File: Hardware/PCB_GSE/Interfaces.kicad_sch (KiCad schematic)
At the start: 32 parts, among them J21 BM03B-GHS-TBT, J3 Screw_Terminal_01x04, J4 GT17HN-4DP-2H(D)(56), J5 Conn_02x07_Odd_Even, J6 Conn_01x02, U5 SI5442DU-T1-GE3, U6 SI5442DU-T1-GE3, U7 SI5442DU-T1-GE3, U8 ISOW1044

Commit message: fix : done silkscreen and finition
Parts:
- renumbered C52 to C1, C50 to C10, C51 to C11, C48 to C12, C53 to C2, C47 to C23, C45 to C25, C55 to C3, C54 to C4, C56 to C5, C46 to C8, C49 to C9, D3 to D1, D1 to D2, FB4 to FB1, J6 to J1, J21 to J2, J4 to J3, J3 to J5, R42 to R1, R40 to R11, R41 to R12, R36 to R14, R38 to R15, R43 to R2, R6 to R3, R7 to R5, U8 to U2, U6 to U3, U7 to U6, U5 to U7, J5 to X1
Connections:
- net GND: no longer J3.5 (Shell)
- no-connect marks 3 -> 4

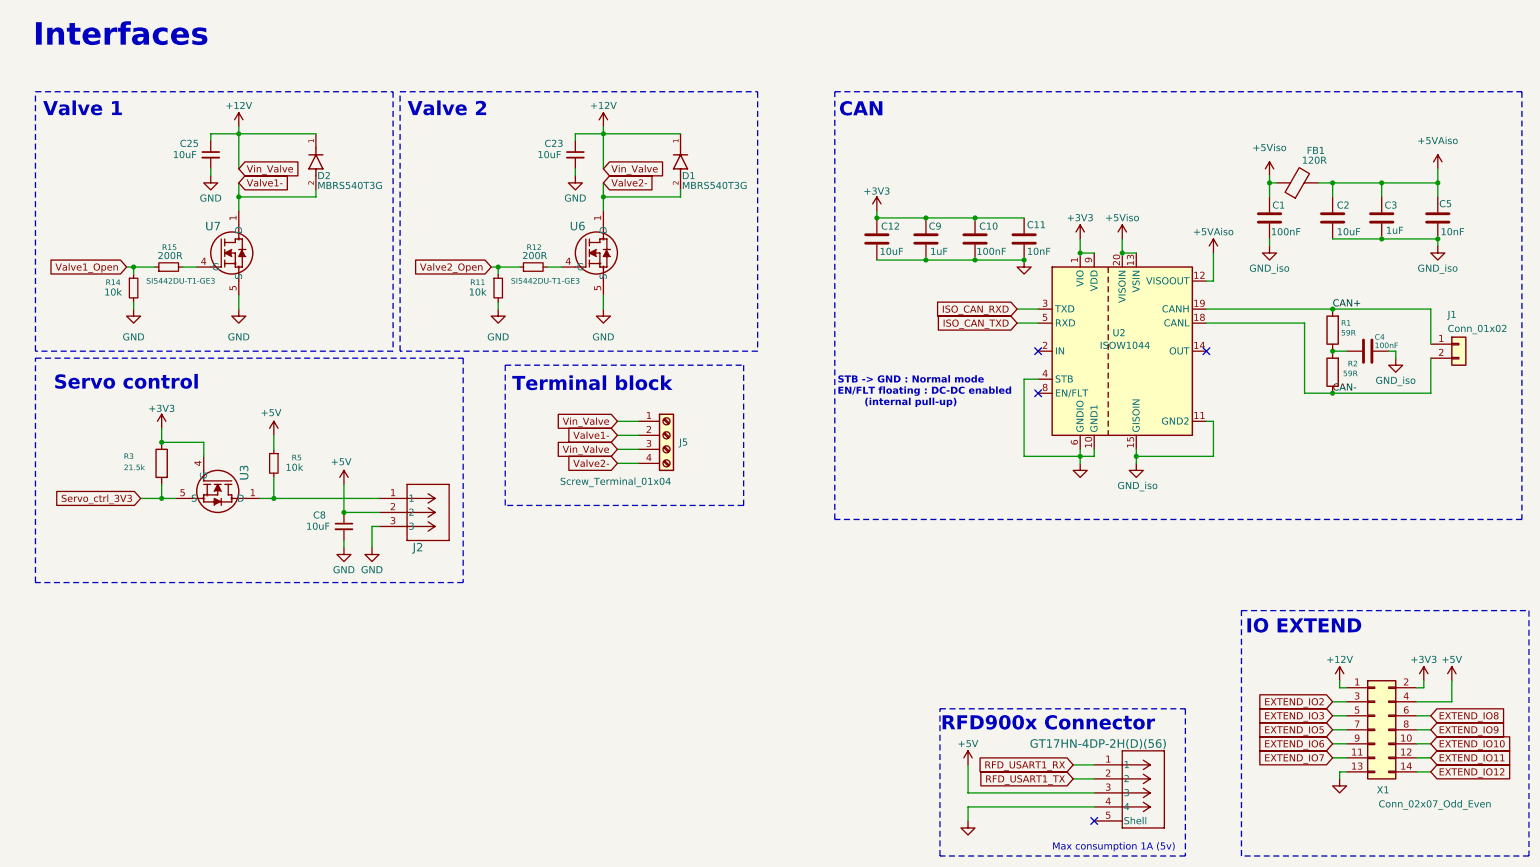
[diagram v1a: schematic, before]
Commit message: fix(gse): Vin servo
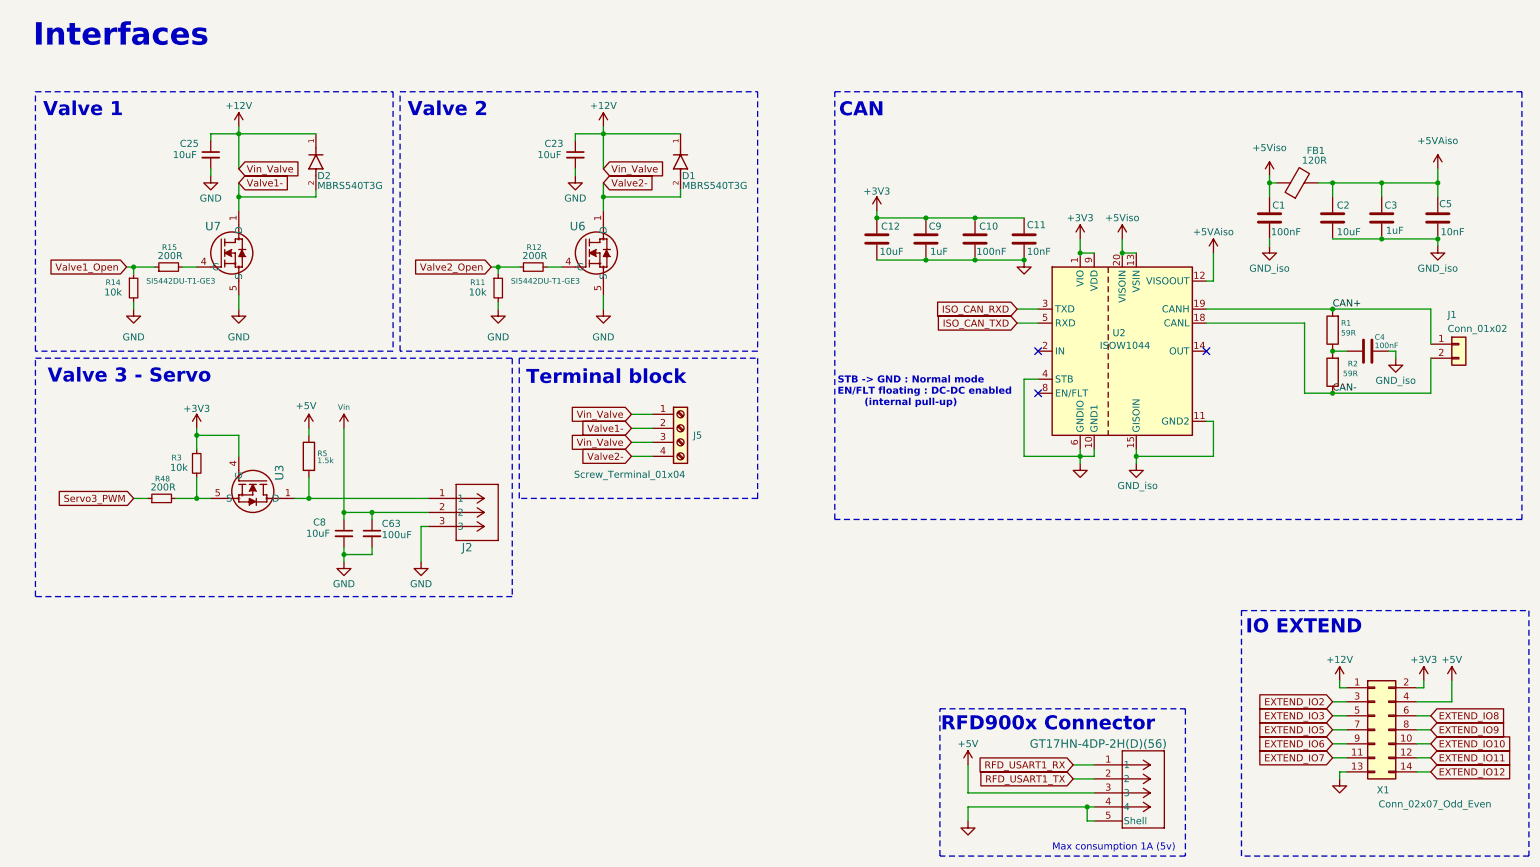
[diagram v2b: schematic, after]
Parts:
- removed R3: 21.5k, Resistor_SMD:R_0805_2012Metric, symbol Device:R
- removed R5: 10k, Resistor_SMD:R_0805_2012Metric, symbol Device:R_Small
- added C63: 100uF, Capacitor_SMD:C_0805_2012Metric, symbol Device:C_Small
- added R3: 10k, Resistor_SMD:R_0805_2012Metric, symbol Device:R_Small
- added R48: 200R, Resistor_SMD:R_0805_2012Metric, symbol Device:R_Small
- added R5: 1.5k, Resistor_SMD:R_0805_2012Metric, symbol Device:R
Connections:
- net +3V3: now also R3.1
- net +5V: now also R5.1; no longer C8.1, J2.2
- net GND: now also J3.5 (Shell), C63.2
- net at J2.1, U3.1 (D), U3.2 (D)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: now also R5.2
- net Servo_ctrl_3V3: no longer names the net of U3.5 (S), U3.9 (S)
- net Servo_ctrl_3V3: now also R3.2, R48.2
- new net Servo3_PWM: R48.1
- new net Vin: C63.1, C8.1, J2.2
- no-connect marks 4 -> 3
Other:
- note added: "Valve 3 - Servo"
- note removed: "Servo control"
- moved on the sheet: C8, J2, J5, U3

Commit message: fix : cap electrolytique servo
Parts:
- C63: footprint Capacitor_SMD:C_0805_2012Metric -> PCB_GSE:U2-K_NCH; DigiKey_Part_Number 1276-2891-1-ND -> 493-3937-1-ND; Manufacturer_Part_Number CL21A106KAYNNNE -> UCL1E101MCL1GS
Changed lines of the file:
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@@
 			)
 		)
-		(property "Footprint" "Capacitor_SMD:C_0805_2012Metric"
+		(property "Footprint" "PCB_GSE:U2-K_NCH"
 			(at 74.93 106.68 0)
 			(effects
@@
 			)
 		)
-		(property "Datasheet" "https://www.digikey.ca/en/products/detail/samsung-electro-mechanics/CL21A106KAYNNNE/3888549"
+		(property "Datasheet" "https://www.digikey.ca/en/products/detail/nichicon/UCL1E101MCL1GS/2300286"
 			(at 74.93 106.68 0)
 			(effects
@@
 			)
 		)
-		(property "DigiKey_Part_Number" "1276-2891-1-ND"
+		(property "DigiKey_Part_Number" "493-3937-1-ND"
 			(at 74.93 106.68 0)
 			(effects
@@
 			)
 		)
-		(property "Manufacturer_Part_Number" "CL21A106KAYNNNE"
+		(property "Manufacturer_Part_Number" "UCL1E101MCL1GS"
 			(at 74.93 106.68 0)
 			(effects

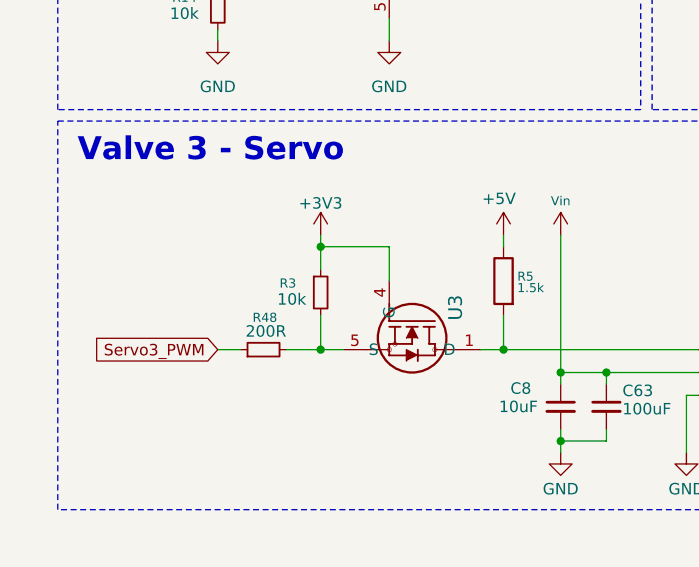
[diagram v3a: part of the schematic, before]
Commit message: fix: silkscreen green<->black + fix silkscreen + connect shield to gnd  in pressure sensor + fix/add doc
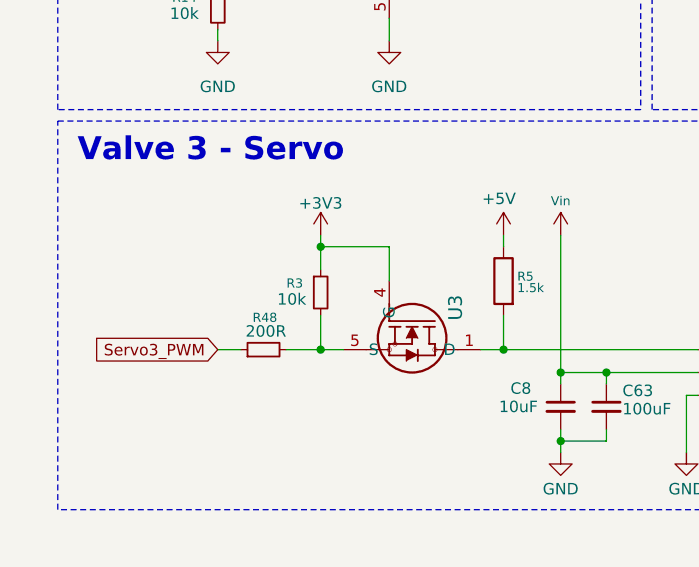
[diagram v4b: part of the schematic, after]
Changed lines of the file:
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@@
 		(dnp no)
 		(property "Reference" "R3"
-			(at 38.608 92.964 0)
+			(at 39.37 92.964 0)
 			(effects
 				(font

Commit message: wip(moteur + gse): fix silkscreen + traces + polygons
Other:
- note added: "*max 7.4V"
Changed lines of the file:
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@@
+		)
+	)
+	(text "*max 7.4V"
+		(exclude_from_sim no)
+		(at 99.568 76.708 0)
+		(effects
+			(font
+				(size 1.27 1.27)
+			)
+			(justify right)
 		)
 	)

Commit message: Fix : servo side connectors
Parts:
- J2: footprint pcb_moteur:CONN_BM03B-GHS-TBT_JST -> pcb_moteur:JST_SM03B-GHS-TB; symbol pcb_moteur:BM03B-GHS-TBT -> PCB_GSE:BM03B-GHS-TBT
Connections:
- no-connect marks 3 -> 4
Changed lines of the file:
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@@
 		(at 195.58 81.28)
 	)
+	(no_connect
+		(at 87.63 107.95)
+	)
 	(wire
 		(pts
@@
 	)
 	(symbol
-		(lib_id "pcb_moteur:BM03B-GHS-TBT")
+		(lib_id "PCB_GSE:BM03B-GHS-TBT")
 		(at 85.09 100.33 0)
 		(unit 1)
@@
 		(dnp no)
 		(property "Reference" "J2"
-			(at 91.186 109.22 0)
+			(at 92.202 96.266 0)
 			(effects
 				(font
@@
 			)
 		)
-		(property "Footprint" "pcb_moteur:CONN_BM03B-GHS-TBT_JST"
+		(property "Footprint" "pcb_moteur:JST_SM03B-GHS-TB"
 			(at 85.09 100.33 0)
 			(effects
@@
 		(pin "2"
 		)
+		(pin "4"
+		)
 		(instances

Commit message: feature : Done v1 and send to fab
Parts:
- removed X1: Conn_02x07_Odd_Even, Connector_PinHeader_2.54mm:PinHeader_2x07_P2.54mm_Vertical, symbol Connector_Generic:Conn_02x07_Odd_Even
- C3, C9: DigiKey_Part_Number 399-C0603C105K4RACTUCT-ND -> 1276-1029-1-ND; Manufacturer_Part_Number C0603C105K4RACTU -> CL21B105KBFNNNE
- J2: value BM03B-GHS-TBT -> SM03B-GHS-TB; DigiKey_Part_Number (none) -> 455-SM03B-GHS-TBCT-ND; Manufacturer_Part_Number (none) -> SM03B-GHS-TB
- R11, R14, R3: DigiKey_Part_Number 311-10.0KHRCT-ND -> 541-10.0KCCT-ND; Manufacturer_Part_Number RC0603FR-0710KL -> CRCW080510K0FKEA
- R5: DigiKey_Part_Number P1.5KDBCT-ND -> 311-1.50KCRCT-ND; Manufacturer_Part_Number ERA-3AEB152V -> RC0805FR-071K5L
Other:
- note removed: "IO EXTEND"
